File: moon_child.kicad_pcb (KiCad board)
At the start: 4 copper layers, 63.2 x 63.2 mm, 185 parts, among them J1 Motor0, J10 USB_C_Receptacle_USB2.0_14P, J2 Motor1, J3 Battery Input, J4 Micro_SD_Card_Det1, J5 Conn_01x04, J6 Conn_01x04, J7 Conn_02x05_Odd_Even, J8 Conn_01x03, J9 debug_probe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

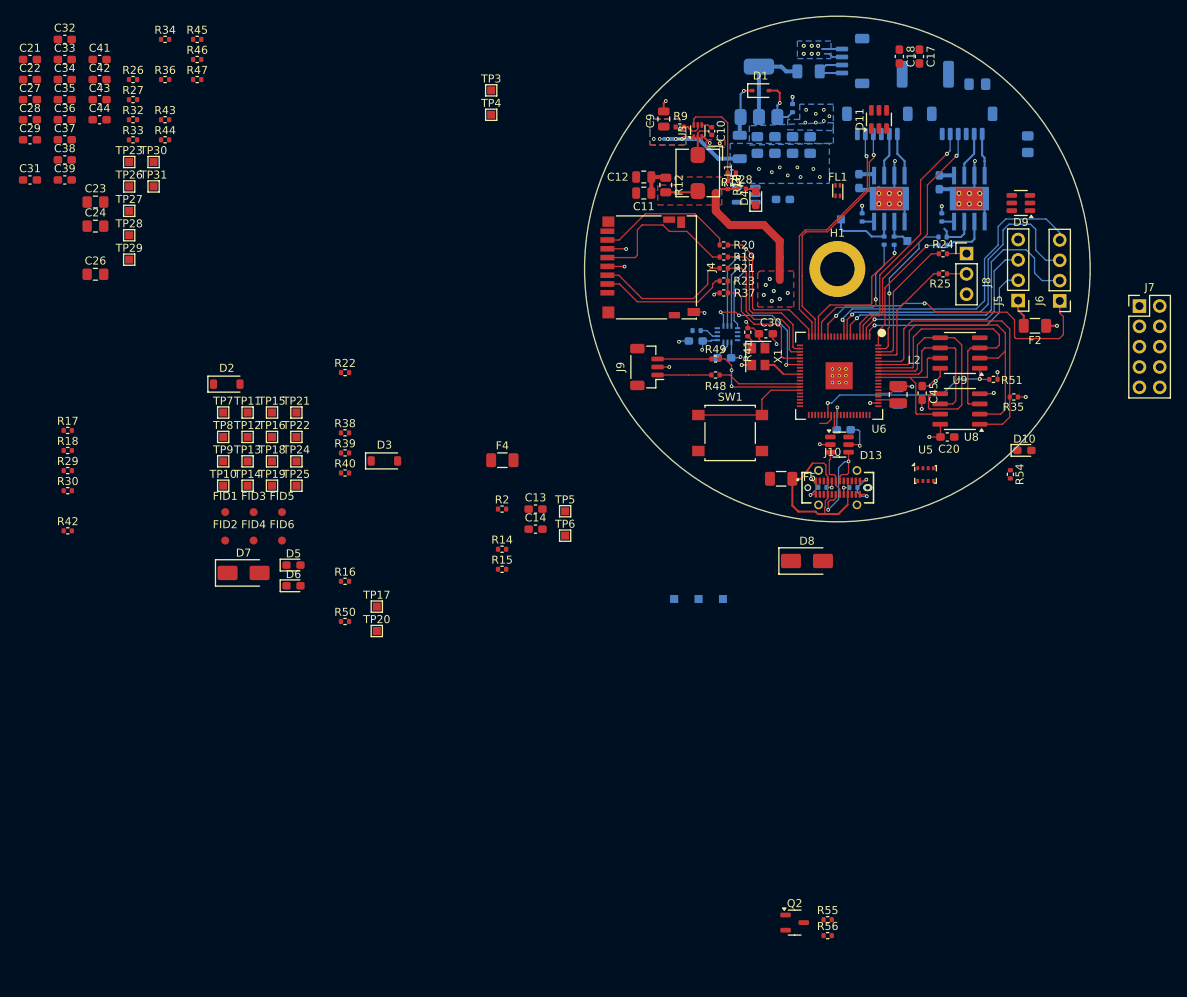
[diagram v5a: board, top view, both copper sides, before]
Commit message: Updates
Routing updates, placed expansion connector.
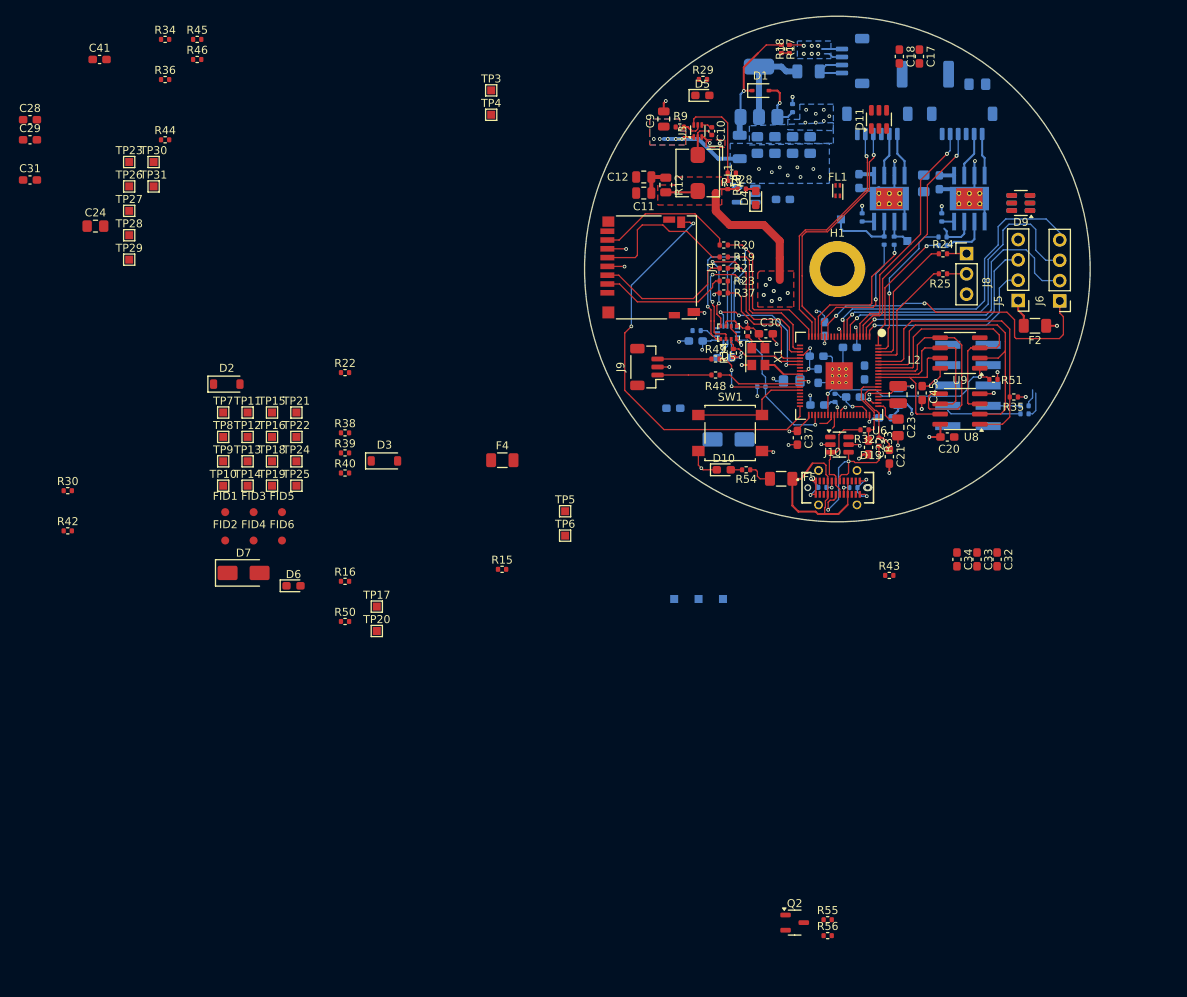
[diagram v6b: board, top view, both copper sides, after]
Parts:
- removed C13, C14: 0.1uF, Capacitor_SMD:C_0603_1608Metric_Pad1.08x0.95mm_HandSolder
- added D12: ESDA6V1BC6, Package_TO_SOT_SMD:SOT-23-6, B.Cu at (182.1, 80.2)
- C26, C27, C35, C36, C38, C39, C42, C43, C44, D8, R2, R26, R27, R47: moved to B.Cu
- J7: footprint Connector_PinHeader_2.54mm:PinHeader_2x05_P2.54mm_Vertical -> Connector_PinHeader_2.54mm:PinHeader_2x05_P2.54mm_Vertical_SMD; moved to B.Cu
- moved C32 133.4 mm to (179.2, 124.8), turned to -90 degrees
- moved C33 130.0 mm to (176.7, 124.8), turned to -90 degrees
- moved C34 126.6 mm to (174.2, 124.8), turned to -90 degrees
- moved R26 119.0 mm to (182.6, 106.6)
- moved C21 118.3 mm to (165.7, 112.0), turned to -90 degrees
- moved R27 117.8 mm to (182.6, 105.6), turned to 180 degrees
- moved C22 114.5 mm to (163.1, 110.8), turned to -90 degrees
- moved C35 110.1 mm to (165.3, 107.1)
- moved R43 107.0 mm to (165.7, 126.8)
- moved C36 104.8 mm to (162.6, 101.4), turned to -90 degrees
- moved C23 104.2 mm to (166.8, 108.3), turned to -90 degrees
- moved R18 103.2 mm to (153.2, 61.0), turned to 90 degrees
- moved C43 101.3 mm to (161.2, 104.5)
- moved R17 101.1 mm to (152.2, 61.0), turned to -90 degrees
- moved R33 100.6 mm to (164.4, 110.1), turned to -90 degrees
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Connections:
- D13 pad 1: /connectors+mechanical/GPS_RX -> unconnected-(D13-TVS1-Pad1)
- D13 pad 6: /connectors+mechanical/GPS_TX -> unconnected-(D13-TVS4-Pad6)
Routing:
- net /raspi/SD_DET: track 0.00 -> 51.9 mm, vias 0 -> 2
- net GND: track 71.9 -> 102.2 mm, vias 37 -> 48
- net 3v3: track 51.2 -> 75.0 mm, vias 18 -> 25
- net /raspi/IMU_INT: track 0.00 -> 18.1 mm, vias 0 -> 1
- net /sensors/MCU_SCLK: track 28.2 -> 43.1 mm, vias 1 -> 2
- net /sensors/MCU_SDI: track 30.0 -> 44.1 mm, vias 1 -> 4
- net /sensors/MCU_SDO: track 25.4 -> 37.8 mm, vias 1 -> 3
- net /raspi/BAR_CS: track 0.00 -> 10.6 mm, vias 0 -> 1
- net Net-(U6-USB_DM): track 0.00 -> 10.5 mm
- net Net-(U6-USB_DP): track 0.00 -> 9.96 mm
- net /raspi/Expansion_RX: track 0.00 -> 9.86 mm
- net Net-(D1-K): track 6.82 -> 15.6 mm
- net /connectors+mechanical/DP+: track 6.21 -> 12.2 mm
- net /connectors+mechanical/DP-: track 14.4 -> 20.2 mm
- net Net-(U6-ADC_AVDD): track 0.00 -> 5.69 mm, vias 0 -> 1
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- added copper zone on In2.Cu, net /raspi/1V1

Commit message: more routing updates
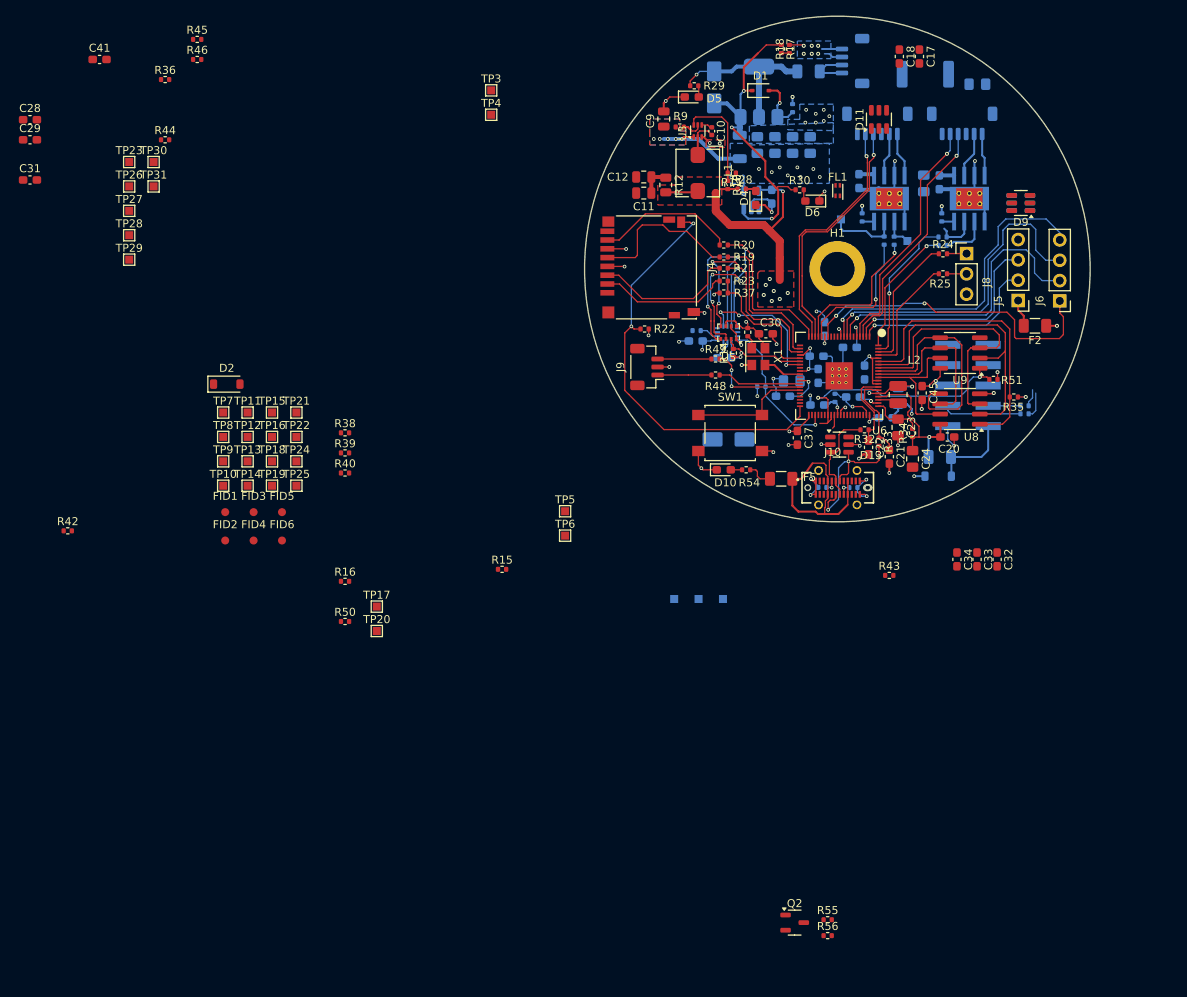
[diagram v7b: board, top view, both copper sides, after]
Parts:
- D3, D7, F4: moved to B.Cu
- moved C24 106.2 mm to (168.6, 112.2), turned to -90 degrees
- moved R34 105.6 mm to (168.6, 109.0), turned to 90 degrees
- moved R30 98.9 mm to (154.5, 78.6)
- moved D7 84.5 mm to (143.8, 65.8), turned to 90 degrees
- moved D6 80.7 mm to (156.1, 80.0), turned to 180 degrees
- moved D3 69.2 mm to (171.8, 114.4), turned to 180 degrees
- moved F4 54.7 mm to (172.0, 112.0)
- moved R22 37.8 mm to (135.1, 96.0), turned to 180 degrees
- moved C27 13.8 mm to (152.4, 104.4)
- moved C19 1.44 mm to (151.0, 79.5), turned to -90 degrees
- moved R29 1.35 mm to (141.3, 65.6)
- moved D5 1.34 mm to (141.0, 67.0)
- moved U7 0.93 mm to (148.4, 79.9), turned to 90 degrees
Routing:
- net 3v3: track 75.0 -> 108.5 mm, vias 25 -> 28
- net Net-(D1-K): track 15.6 -> 41.9 mm, vias 1 -> 3
- net GND: track 102.2 -> 121.1 mm, vias 48 -> 52
- net Net-(D3-K): track 0.00 -> 10.4 mm
- net Net-(D7-A): track 11.3 -> 21.3 mm, vias 0 -> 1
- net /raspi/1V1: track 11.2 -> 14.7 mm
- net /raspi/QSPI_BK_SS: track 26.1 -> 28.9 mm
- net Net-(U6-VREG_AVDD): track 3.65 -> 6.39 mm
- net Board_VBATT: track 15.9 -> 17.9 mm
- net Net-(D6-A): track 0.00 -> 1.48 mm
- net Net-(D5-A): track 0.00 -> 1.42 mm
- net /raspi/SD_DET: track 51.9 -> 53.2 mm

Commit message: layout updates
Updated encoder, esd and other layouts
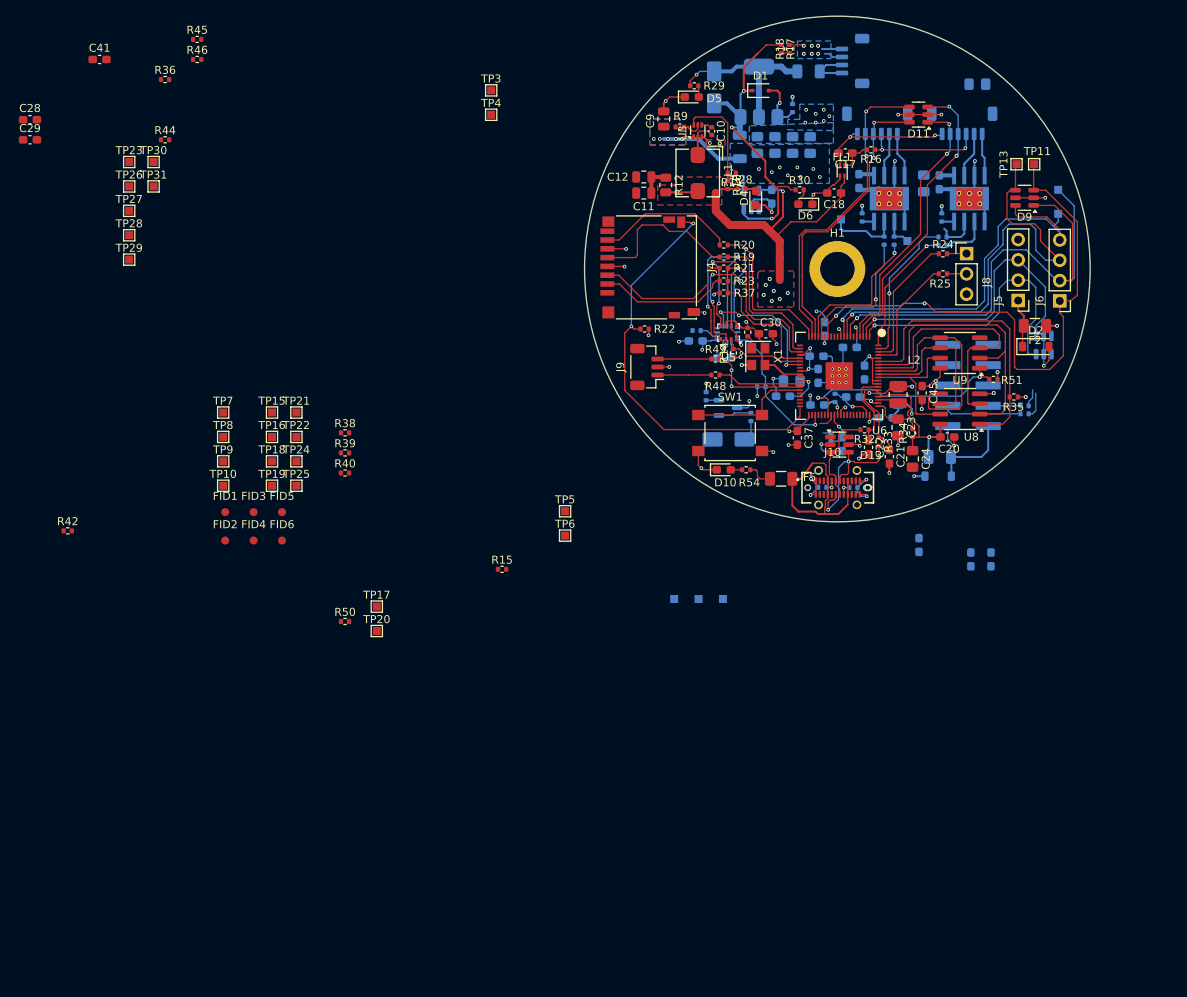
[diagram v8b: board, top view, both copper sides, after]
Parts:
- removed FB1: DNP, Inductor_SMD:L_2512_6332Metric
- C31, C32, C33, C34, Q2, R43, R55, R56, TP12, TP14: moved to B.Cu
- moved TP14 106.9 mm to (186.8, 81.6), turned to 180 degrees
- moved C31 106.8 mm to (159.8, 110.4), turned to -90 degrees
- moved TP12 105.9 mm to (186.8, 78.6), turned to 180 degrees
- moved TP11 103.1 mm to (183.8, 75.4)
- moved TP13 103.0 mm to (181.6, 75.4)
- moved D2 101.2 mm to (184.0, 98.2)
- moved R16 85.0 mm to (163.4, 73.6), turned to 180 degrees
- moved R55 67.2 mm to (142.8, 104.4), turned to -90 degrees
- moved R56 65.5 mm to (148.4, 107.0), turned to -90 degrees
- moved Q2 64.9 mm to (145.5, 105.8)
- moved C18 18.9 mm to (158.8, 79.0), turned to 180 degrees
- moved R43 18.8 mm to (158.4, 109.5), turned to 90 degrees
- moved D12 18.0 mm to (185.0, 98.0), turned to 90 degrees
- moved C17 15.2 mm to (160.2, 74.0), turned to 180 degrees
- moved C34 5.08 mm to (169.4, 123.0)
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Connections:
- D11 pad 1: /connectors+mechanical/Encoder1_A -> /connectors+mechanical/Encoder1_B
- D11 pad 3: /connectors+mechanical/Encoder1_B -> /connectors+mechanical/Encoder1_A
- D11 pad 4: /connectors+mechanical/Encoder0_A -> /connectors+mechanical/Encoder0_B
- D11 pad 6: /connectors+mechanical/Encoder0_B -> /connectors+mechanical/Encoder0_A
- D9 pad 1: /connectors+mechanical/GPS_PPS -> /connectors+mechanical/GPS_RESET
- D9 pad 3: /connectors+mechanical/GPS_RESET -> /connectors+mechanical/GPS_PPS
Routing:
- net /connectors+mechanical/GPS_PPS: track 39.8 -> 68.7 mm
- net /connectors+mechanical/GPS_RESET: track 37.7 -> 64.9 mm
- net GND: track 121.1 -> 146.5 mm, vias 52 -> 57
- net /connectors+mechanical/GPS_SAFE: track 41.4 -> 58.6 mm
- net Encoder_GND: track 0.00 -> 16.9 mm, vias 0 -> 2
- net Encoder_VCC: track 0.00 -> 15.2 mm, vias 0 -> 2
- net 3v3: track 108.5 -> 122.7 mm, vias 28 -> 29
- net /connectors+mechanical/GPS_RX: track 23.7 -> 36.0 mm
- net /connectors+mechanical/GPS_TX: track 26.6 -> 38.0 mm
- net /connectors+mechanical/GPS_INT: track 40.7 -> 51.2 mm
- net /connectors+mechanical/Encoder0_B: track 31.2 -> 39.7 mm, vias 1 -> 2
- net /connectors+mechanical/Encoder1_A: track 30.8 -> 37.4 mm, vias 1 -> 2
- net /connectors+mechanical/Encoder0_A: track 31.3 -> 37.2 mm, vias 1 -> 2
- net Net-(C17-Pad1): track 0.00 -> 4.20 mm
- net Net-(Q2-B): track 0.00 -> 4.13 mm
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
